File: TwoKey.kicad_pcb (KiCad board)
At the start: 2 copper layers, 39.1 x 31.9 mm, 33 parts, among them J1 USB_C_Receptacle_USB2.0, SW1 SW_SPST, SW2 SW_SPST, SW3 BOOTSEL, U1 AMS1117-3.3, U2 W25Q128JVS, U3 RP2040TR7, X1 OSC

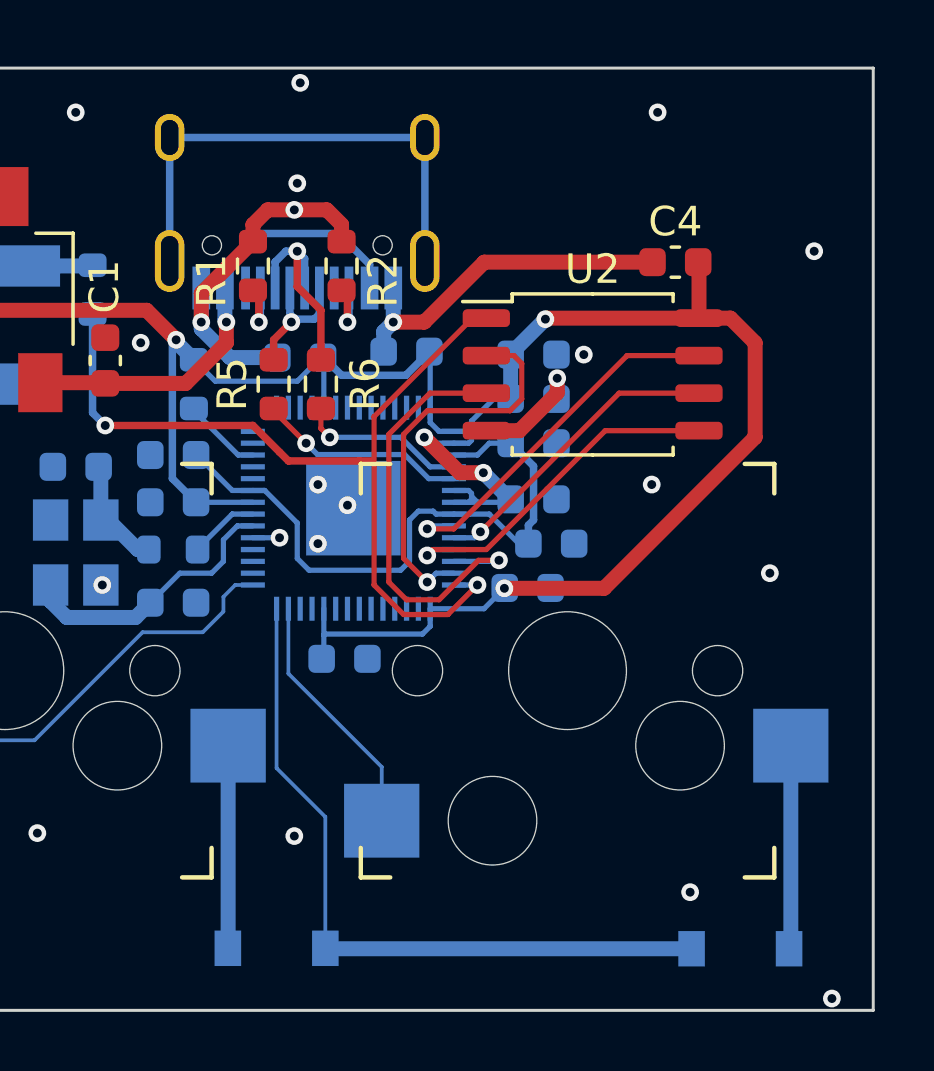
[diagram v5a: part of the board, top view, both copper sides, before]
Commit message: Finished routing some traces
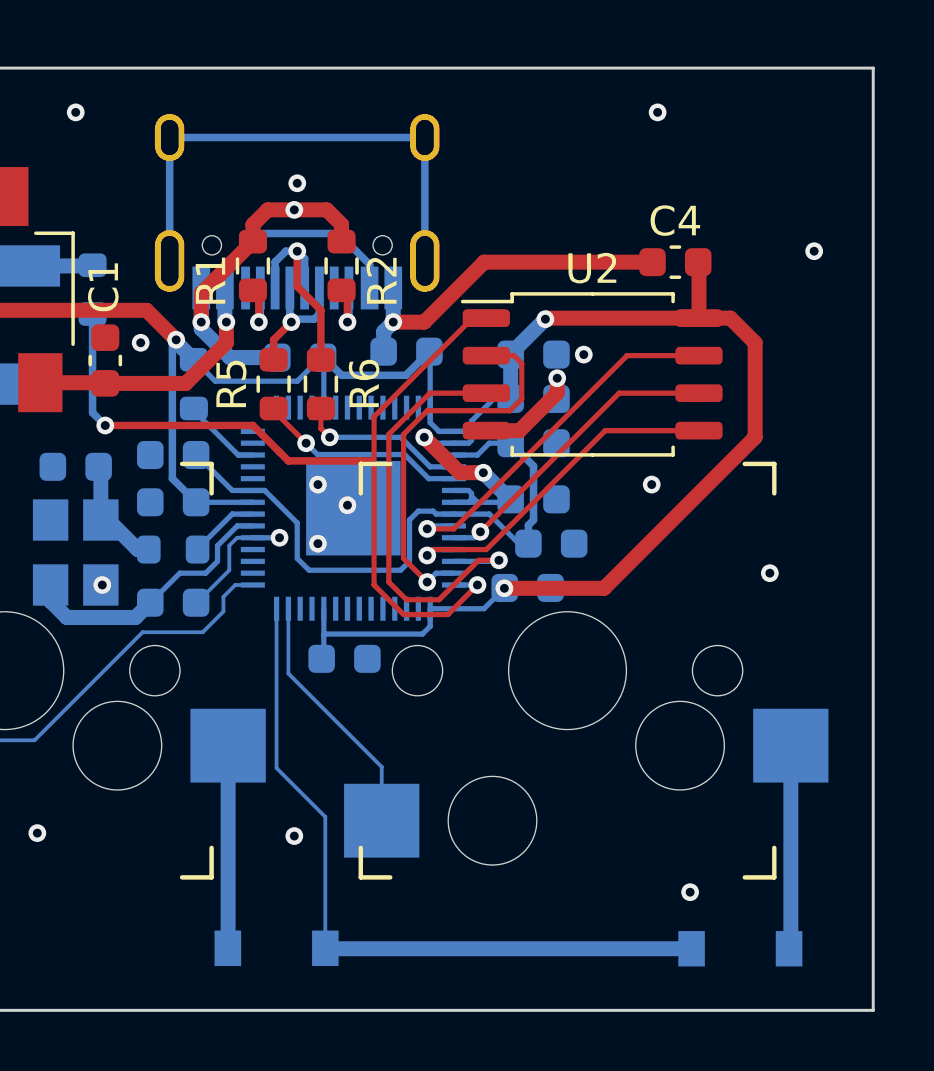
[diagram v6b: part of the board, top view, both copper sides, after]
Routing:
- net GND: track 28.6 -> 31.9 mm, vias 25 -> 23
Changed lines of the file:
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@@
       (outputformat 1)
       (mirror false)
-      (drillshape 1)
+      (drillshape 0)
       (scaleselection 1)
       (outputdirectory "")
@@
   (segment (start 53.05 56.4) (end 54.1 56.4) (width 0.508) (layer "F.Cu") (net 2))
   (via (at 46.55 56.4) (size 0.6) (drill 0.3) (layers "F.Cu" "B.Cu") (net 2))
-  (via (at 67.9 79.3) (size 0.6) (drill 0.3) (layers "F.Cu" "B.Cu") (free) (net 2))
   (via (at 33.9 50.1) (size 0.6) (drill 0.3) (layers "F.Cu" "B.Cu") (free) (net 2))
   (via (at 49.8 51.7) (size 0.6) (drill 0.3) (layers "F.Cu" "B.Cu") (free) (net 2))
@@
   (via (at 43.2 65.3) (size 0.6) (drill 0.3) (layers "F.Cu" "B.Cu") (net 2))
   (via (at 44.5 57.1) (size 0.6) (drill 0.3) (layers "F.Cu" "B.Cu") (free) (net 2))
-  (via (at 49.9 48.3) (size 0.6) (drill 0.3) (layers "F.Cu" "B.Cu") (free) (net 2))
   (via (at 58.6 58.3) (size 0.6) (drill 0.3) (layers "F.Cu" "B.Cu") (free) (net 2))
   (via (at 36.1 79.1) (size 0.6) (drill 0.3) (layers "F.Cu" "B.Cu") (free) (net 2))
@@
   (via (at 41 73.7) (size 0.6) (drill 0.3) (layers "F.Cu" "B.Cu") (free) (net 2))
   (segment (start 47.520979 57.6) (end 49.125 57.6) (width 0.508) (layer "B.Cu") (net 2))
+  (segment (start 47.76473 63.700125) (end 48.2964 63.700125) (width 0.127) (layer "B.Cu") (net 2))
   (segment (start 52.725 57.4) (end 52.725 56.725) (width 0.508) (layer "B.Cu") (net 2))
+  (segment (start 46.4 65.9) (end 47.5 64.8) (width 0.127) (layer "B.Cu") (net 2))
   (segment (start 46.55 56.629021) (end 47.520979 57.6) (width 0.508) (layer "B.Cu") (net 2))
   (segment (start 46.55 55.245) (end 46.55 56.4) (width 0.508) (layer "B.Cu") (net 2))
   (segment (start 48.2964 63.700125) (end 49.199875 63.700125) (width 0.1778) (layer "B.Cu") (net 2))
   (segment (start 46.55 56.4) (end 46.55 56.629021) (width 0.508) (layer "B.Cu") (net 2))
+  (segment (start 47.5 63.964855) (end 47.76473 63.700125) (width 0.127) (layer "B.Cu") (net 2))
+  (segment (start 46.375 65.9) (end 46.4 65.9) (width 0.127) (layer "B.Cu") (net 2))
+  (segment (start 47.5 64.8) (end 47.5 63.964855) (width 0.127) (layer "B.Cu") (net 2))
   (segment (start 52.725 56.725) (end 53.05 56.4) (width 0.508) (layer "B.Cu") (net 2))
   (segment (start 53.05 55.245) (end 53.05 56.4) (width 0.508) (layer "B.Cu") (net 2))
@@
   (segment (start 55.7 60.2) (end 55.7 60) (width 0.1778) (layer "B.Cu") (net 3))
   (segment (start 55.1036 62.499975) (end 55.600025 62.499975) (width 0.1778) (layer "B.Cu") (net 3))
-  (segment (start 47.3 64.5) (end 47.3 63.770403) (width 0.1778) (layer "B.Cu") (net 4))
-  (segment (start 45.825 64.9) (end 46.9 64.9) (width 0.1778) (layer "B.Cu") (net 4))
-  (segment (start 46.9 64.9) (end 47.3 64.5) (width 0.1778) (layer "B.Cu") (net 4))
-  (segment (start 47.3 63.770403) (end 47.770328 63.300075) (width 0.1778) (layer "B.Cu") (net 4))
+  (segment (start 44.825 65.9) (end 45.825 64.9) (width 0.1778) (layer "B.Cu") (net 4))
+  (segment (start 45.825 64.9) (end 46.7 64.9) (width 0.1778) (layer "B.Cu") (net 4))
+  (segment (start 47.1 64.5) (end 47.1 63.970403) (width 0.1778) (layer "B.Cu") (net 4))
   (segment (start 44.325 66.4) (end 44.825 65.9) (width 0.508) (layer "B.Cu") (net 4))
-  (segment (start 47.770328 63.300075) (end 48.2964 63.300075) (width 0.1778) (layer "B.Cu") (net 4))
   (segment (start 41.45 65.85) (end 42 66.4) (width 0.508) (layer "B.Cu") (net 4))
   (segment (start 42 66.4) (end 44.325 66.4) (width 0.508) (layer "B.Cu") (net 4))
-  (segment (start 44.825 65.9) (end 45.825 64.9) (width 0.1778) (layer "B.Cu") (net 4))
+  (segment (start 46.7 64.9) (end 47.1 64.5) (width 0.1778) (layer "B.Cu") (net 4))
   (segment (start 41.45 65.3) (end 41.45 65.85) (width 0.508) (layer "B.Cu") (net 4))
+  (segment (start 47.770328 63.300075) (end 48.2964 63.300075) (width 0.1778) (layer "B.Cu") (net 4))
+  (segment (start 47.1 63.970403) (end 47.770328 63.300075) (width 0.1778) (layer "B.Cu") (net 4))
   (segment (start 43.15 61.375) (end 43.075 61.3) (width 0.508) (layer "B.Cu") (net 5))
   (segment (start 44.4 64.1) (end 44.775 64.1) (width 0.508) (layer "B.Cu") (net 5))
